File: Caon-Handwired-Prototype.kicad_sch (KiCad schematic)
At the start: 176 parts, among them J1 OLED_128x32, SW30 EC11 ENCODER 1, SW45 EC11 ENCODER 1, U1 74HC595, U2 74HC595, U3 SuperMini nRF52840

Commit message: Update
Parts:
- removed D59: ~, Caon_Footprint:D_DO-35_SOD27_P2.54mm_Caon65, symbol Diode:1N4148
- removed SW59: ~, Caon_Footprint:SW_PUSH_6mm, symbol Switch:SW_Push_45deg
- renumbered D60 to D59, D61 to D60, D62 to D61, D63 to D62, D64 to D63, D65 to D64, D66 to D65, D67 to D66, D68 to D67, D69 to D68, D70 to D69, D71 to D70, D72 to D71, D73 to D72, D74 to D73, D75 to D74, SW60 to SW59, SW61 to SW60, SW62 to SW61, SW63 to SW62, SW64 to SW63, SW65 to SW64, SW66 to SW65, SW67 to SW66, SW68 to SW67, SW69 to SW68, SW70 to SW69, SW71 to SW70, SW72 to SW71, SW73 to SW72, SW74 to SW73, SW75 to SW74
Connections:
- net C13: now also SW59.1
- net C14: no longer SW59.1
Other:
- moved on the sheet: D59, SW59

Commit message: Update
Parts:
- RST1: footprint (none) -> Button_Switch_Keyboard:SW_Cherry_MX_1.00u_Plate
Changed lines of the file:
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@@
 			)
 		)
-		(property "Footprint" ""
+		(property "Footprint" "Button_Switch_Keyboard:SW_Cherry_MX_1.00u_Plate"
 			(at 322.58 96.52 0)
 			(effects

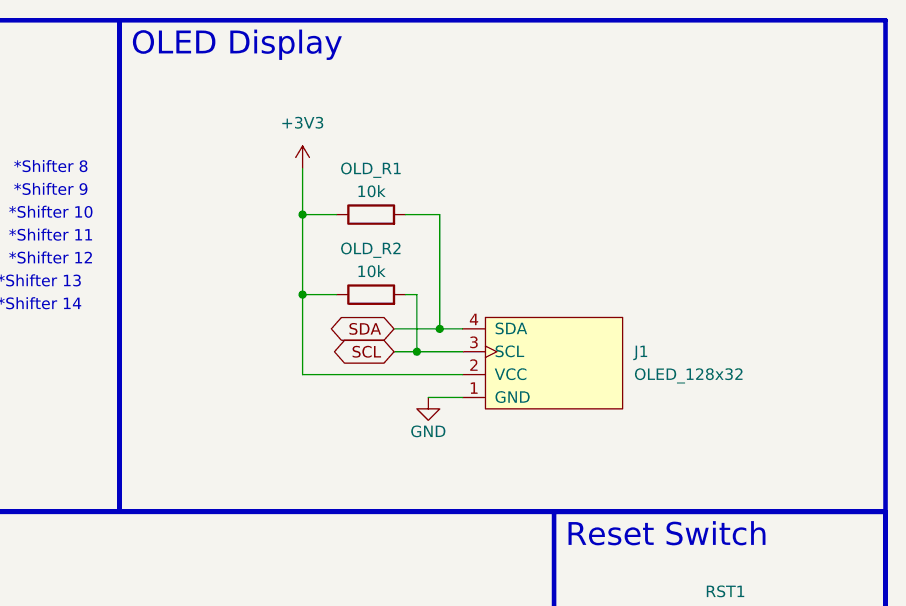
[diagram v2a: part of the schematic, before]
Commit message: Oled protection circuits
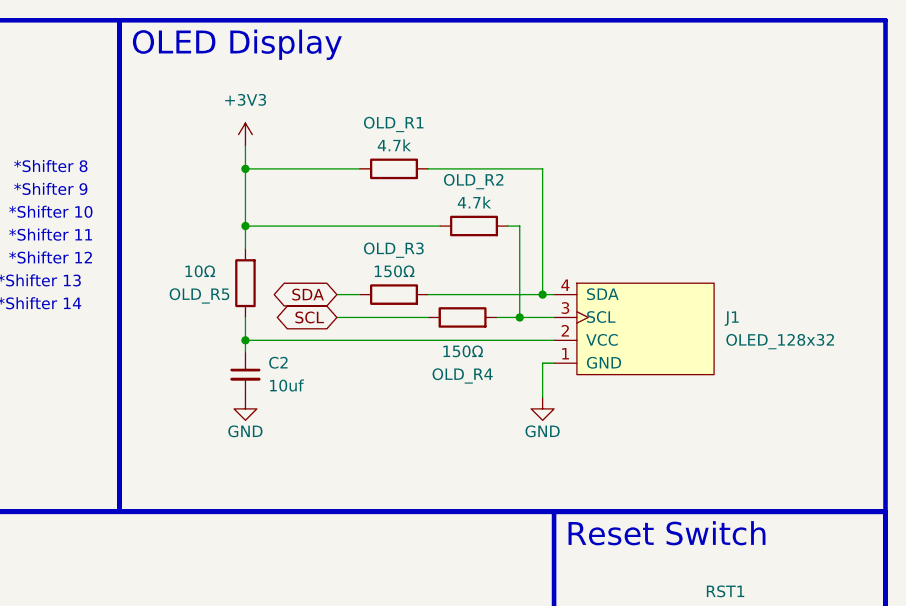
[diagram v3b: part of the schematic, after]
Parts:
- added C2: 10uf, symbol Device:C_Small
- added OLD_R3, OLD_R4: 150Ω, Resistor_THT:R_Axial_DIN0204_L3.6mm_D1.6mm_P2.54mm_Vertical, symbol Device:R
- added OLD_R5: 10Ω, Resistor_THT:R_Axial_DIN0204_L3.6mm_D1.6mm_P2.54mm_Vertical, symbol Device:R
- OLD_R1, OLD_R2: value 10k -> 4.7k
- SW1, SW10, SW11, SW12, SW13, SW14, SW15, SW16, SW17, SW18, SW19, SW2, SW20, SW21, SW22, SW23, SW24, SW25, SW26, SW27, SW28, SW29, SW3, SW31, SW32, SW33, SW34, SW35, SW36, SW37, SW38, SW39, SW4, SW40, SW41, SW42, SW43, SW44, SW46, SW47, SW48, SW49, SW5, SW50, SW51, SW52, SW53, SW54, SW55, SW56, SW57, SW58, SW59, SW6, SW60, SW61, SW62, SW63, SW64, SW65, SW66, SW67, SW68, SW69, SW7, SW70, SW71, SW72, SW73, SW74, SW8, SW9: footprint Caon_Footprint:SW_PUSH_6mm -> Caon_Footprint:Hotswap_MX_Plated_1u
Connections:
- net +3V3: now also OLD_R5.2; no longer J1.2 (VCC)
- net GND: now also C2.2
- net SCL: now also OLD_R4.1; no longer J1.3 (SCL), OLD_R2.2
- net SDA: now also OLD_R3.1; no longer J1.4 (SDA), OLD_R1.2
- new net: C2.1, J1.2 (VCC), OLD_R5.1
- new net: J1.3 (SCL), OLD_R2.2, OLD_R4.2
- new net: J1.4 (SDA), OLD_R1.2, OLD_R3.2
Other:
- moved on the sheet: J1, OLD_R1, OLD_R2

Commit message: Updated OLED protection circuit
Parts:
- added C1: 0.1uf, symbol Device:C_Small
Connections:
- net GND: now also C1.2
- net at C2.1, J1.2 (VCC), OLD_R5.1: now also C1.1
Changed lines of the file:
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@@
 	)
 	(junction
+		(at 280.67 68.58)
+		(diameter 0)
+		(color 0 0 0 0)
+	)
+	(junction
 		(at 157.48 189.23)
 		(diameter 0)
@@
 	(wire
 		(pts
-			(xy 269.24 68.58) (xy 303.53 68.58)
+			(xy 269.24 68.58) (xy 280.67 68.58)
 		)
 		(stroke
@@
 	(wire
 		(pts
+			(xy 280.67 68.58) (xy 303.53 68.58)
+		)
+		(stroke
+			(width 0)
+			(type default)
+		)
+	)
+	(wire
+		(pts
 			(xy 125.73 143.51) (xy 138.43 143.51)
 		)
@@
 	(wire
 		(pts
+			(xy 280.67 68.58) (xy 280.67 69.85)
+		)
+		(stroke
+			(width 0)
+			(type default)
+		)
+	)
+	(wire
+		(pts
 			(xy 190.5 261.62) (xy 190.5 262.89)
 		)
@@
 	)
 	(symbol
+		(lib_id "Device:C_Small")
+		(at 280.67 72.39 0)
+		(unit 1)
+		(exclude_from_sim no)
+		(in_bom yes)
+		(on_board yes)
+		(dnp no)
+		(property "Reference" "C1"
+			(at 283.21 71.12 0)
+			(effects
+				(font
+					(size 1.27 1.27)
+				)
+				(justify left)
+			)
+		)
+		(property "Value" "0.1uf"
+			(at 283.21 73.66 0)
+			(effects
+				(font
+					(size 1.27 1.27)
+				)
+				(justify left)
+			)
+		)
+		(property "Footprint" ""
+			(at 280.67 72.39 0)
+			(effects
+				(font
+					(size 1.27 1.27)
+				)
+				(hide yes)
+			)
+		)
+		(property "Datasheet" "~"
+			(at 280.67 72.39 0)
+			(effects
+				(font
+					(size 1.27 1.27)
+				)
+				(hide yes)
+			)
+		)
+		(property "Description" "Unpolarized capacitor, small symbol"
+			(at 280.67 72.39 0)
+			(effects
+				(font
+					(size 1.27 1.27)
+				)
+				(hide yes)
+			)
+		)
+		(pin "1"
+		)
+		(pin "2"
+		)
+		(instances
+			(project "Caon-Handwired-Prototype"
+				(path "/8df2f29a-df03-4271-980f-9b5acafffeb5"
+					(reference "C1")
+					(unit 1)
+				)
+			)
+		)
+	)
+	(symbol
 		(lib_id "PCM_marbastlib-promicroish:SuperMini_nRF52840")
 		(at 78.74 63.5 0)
@@
 					(unit 1)
 				)
+			)
+		)
+	)
+	(symbol
+		(lib_id "power:GND")
+		(at 280.67 74.93 0)
+		(unit 1)
+		(exclude_from_sim no)
+		(in_bom yes)
+		(on_board yes)
+		(dnp no)
+		(property "Reference" "#PWR016"
+			(at 280.67 81.28 0)
+			(effects
+				(font
+					(size 1.27 1.27)
+				)
+				(hide yes)
+			)
+		)
+		(property "Value" "GND"
+			(at 280.67 78.74 0)
+			(effects
+				(font
+					(size 1.27 1.27)
+				)
+			)
+		)
+		(property "Footprint" ""
+			(at 280.67 74.93 0)
+			(effects
+				(font
+					(size 1.27 1.27)
+				)
+				(hide yes)
+			)
+		)
+		(property "Datasheet" ""
+			(at 280.67 74.93 0)
+			(effects
+				(font
+					(size 1.27 1.27)
+				)
+				(hide yes)
+			)
+		)
+		(property "Description" "Power symbol creates a global label with name \"GND\" , ground"
+			(at 280.67 74.93 0)
+			(effects
+				(font
+					(size 1.27 1.27)
+				)
+				(hide yes)
+			)
+		)
+		(pin "1"
+		)
+		(instances
+			(project "Caon-Handwired-Prototype"
+				(path "/8df2f29a-df03-4271-980f-9b5acafffeb5"
+					(reference "#PWR016")
+					(unit 1)
+				)

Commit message: Readibility
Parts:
- renumbered C2 to C1, C1 to C2, OLD_R5 to OLD_R3, OLD_R3 to OLD_R4, OLD_R4 to OLD_R5
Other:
- moved on the sheet: C1, C2, J1, OLD_R1, OLD_R2, OLD_R3, OLD_R4, OLD_R5

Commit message: Oled Protection ciruit
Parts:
- removed OLD_R3: 10Ω, Resistor_THT:R_Axial_DIN0204_L3.6mm_D1.6mm_P2.54mm_Vertical, symbol Device:R
- OLD_R4, OLD_R5: value 150Ω -> 100Ω
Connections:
- net +3V3: now also C1.1, C2.1, J1.2 (VCC)
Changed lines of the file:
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@@
 	(wire
 		(pts
-			(xy 264.16 53.34) (xy 264.16 58.42)
-		)
-		(stroke
-			(width 0)
-			(type default)
-		)
-	)
-	(wire
-		(pts
 			(xy 125.73 172.72) (xy 125.73 173.99)
 		)
@@
 	(wire
 		(pts
-			(xy 264.16 66.04) (xy 264.16 72.39)
+			(xy 264.16 53.34) (xy 264.16 72.39)
 		)
 		(stroke
@@
 	)
 	(image
-		(at 213.36 341.63)
+		(at 250.19 342.9)
 		(scale 4.87792)
 		(data "iVBORw0KGgoAAAANSUhEUgAAA2oAAAEfCAIAAAC/OaIHAAAAA3NCSVQICAjb4U/gAAAgAElEQVR4"
@@
 			)
 		)
-		(property "Value" "150Ω"
+		(property "Value" "100Ω"
 			(at 288.29 63.5 90)
 			(effects
@@
 			)
 		)
-		(property "Value" "150Ω"
+		(property "Value" "100Ω"
 			(at 307.34 58.42 90)
 			(effects
@@
 					(unit 1)
 				)
-			)
-		)
-	)
-	(symbol
-		(lib_id "Device:R")
-		(at 264.16 62.23 180)
-		(unit 1)
-		(exclude_from_sim no)
-		(in_bom yes)
-		(on_board yes)
-		(dnp no)
-		(property "Reference" "OLD_R3"
-			(at 266.7 63.5 0)
-			(effects
-				(font
-					(size 1.27 1.27)
-				)
-				(justify right)
-			)
-		)
-		(property "Value" "10Ω"
-			(at 266.7 60.96 0)
-			(effects
-				(font
-					(size 1.27 1.27)
-				)
-				(justify right)
-			)
-		)
-		(property "Footprint" "Resistor_THT:R_Axial_DIN0204_L3.6mm_D1.6mm_P2.54mm_Vertical"
-			(at 265.938 62.23 90)
-			(effects
-				(font
-					(size 1.27 1.27)
-				)
-				(hide yes)
-			)
-		)
-		(property "Datasheet" "~"
-			(at 264.16 62.23 0)
-			(effects
-				(font
-					(size 1.27 1.27)
-				)
-				(hide yes)
-			)
-		)
-		(property "Description" "Resistor"
-			(at 264.16 62.23 0)
-			(effects
-				(font
-					(size 1.27 1.27)
-				)
-				(hide yes)
-			)
-		)
-		(pin "1"
-		)
-		(pin "2"
-		)
-		(instances
-			(project "Caon-Handwired-Prototype"
-				(path "/8df2f29a-df03-4271-980f-9b5acafffeb5"
-					(reference "OLD_R3")
-					(unit 1)
-				)

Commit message: decaps on shifter
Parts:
- added C3, C5: 10uf, symbol Device:C_Small
- added C4, C6: 0.1uf, symbol Device:C_Small
- renumbered OLD_R4 to OLD_R3, OLD_R5 to OLD_R4
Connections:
- net +3V3: now also C3.1, C4.1, C5.1, C6.1
- net GND: now also C3.2, C4.2, C5.2, C6.2
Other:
- moved on the sheet: OLD_R3, OLD_R4, RST1, S_D1, S_D10, S_D11, S_D12, S_D13, S_D14, S_D15, S_D2, S_D3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
